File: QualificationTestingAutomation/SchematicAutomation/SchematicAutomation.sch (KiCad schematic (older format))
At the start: 0 parts

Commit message: schematic is finished a few symbols were added, footprints are almost done, some work needs to be done on the connectors#
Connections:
- net labels added: +5V
- wire segments 0 -> 22
- no-connect marks 0 -> 1
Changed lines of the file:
@@
 $Descr B 17000 11000
 encoding utf-8
-Sheet 1 6
+Sheet 1 18
 Title ""
 Date ""
@@
 $EndDescr
 $Sheet
-S 1350 700  3600 2900
+S 1350 650  3600 2900
 U 5B9C8971
 F0 "IO" 50
@@
 $EndSheet
 $Sheet
-S 6100 800  4400 2800
+S 5450 700  4400 2800
 U 5B9C8983
 F0 "MUXing" 50
@@
 $EndSheet
 $Sheet
-S 11650 1000 4300 2550
+S 10400 900  4300 2550
 U 5B9C8995
-F0 "MSP430" 50
-F1 "MSP430.sch" 50
+F0 "ATMEGA2560" 50
+F1 "ATMEGA2560.sch" 50
+F2 "VBUS" I R 14700 1850 50
+F3 "D+" I R 14700 2000 50
+F4 "D-" I R 14700 2150 50
 $EndSheet
 $Sheet
@@
 $EndSheet
 $Sheet
-S 6750 5450 3900 3100
+S 5750 5350 3900 3100
 U 5BCA1CB6
 F0 "MUXing-2" 50
 F1 "MUXing-2.sch" 50
 $EndSheet
+$Sheet
+S 10050 4850 4000 2350
+U 5BB9E3C7
+F0 "RS232" 50
+F1 "RS232.sch" 50
+F2 "DM_1" I R 14050 5900 50
+F3 "DP_1" I R 14050 5800 50
+F4 "DM_2" I R 14050 6250 50
+F5 "DP_2" I R 14050 6350 50
+F6 "DP_3" I R 14050 6550 50
+F7 "DM_3" I R 14050 6650 50
+$EndSheet
+$Sheet
+S 15050 5450 2600 1600
+U 5BE528E5
+F0 "USBInterface" 50
+F1 "USB.sch" 50
+F2 "DM1" I L 15050 5900 50
+F3 "DP1" I L 15050 6000 50
+F4 "DM2" I L 15050 6150 50
+F5 "DP2" I L 15050 6300 50
+F6 "DP3" I L 15050 6550 50
+F7 "DM3" I L 15050 6650 50
+F8 "DP4" I L 15050 5550 50
+F9 "DM4" I L 15050 5650 50
+$EndSheet
+Wire Wire Line
+	14700 2150 14550 2150
+Wire Wire Line
+	14550 2150 14550 5650
+Wire Wire Line
+	14550 5650 15050 5650
+Wire Wire Line
+	15050 5550 14850 5550
+Wire Wire Line
+	14850 5550 14850 2000
+Wire Wire Line
+	14850 2000 14700 2000
+Wire Wire Line
+	15050 5900 14450 5900
+Wire Wire Line
+	14450 5900 14450 5800
+Wire Wire Line
+	14450 5800 14050 5800
+Wire Wire Line
+	15050 6000 14350 6000
+Wire Wire Line
+	14350 6000 14350 5900
+Wire Wire Line
+	14350 5900 14050 5900
+Wire Wire Line
+	15050 6150 14150 6150
+Wire Wire Line
+	14150 6150 14150 6250
+Wire Wire Line
+	14150 6250 14050 6250
+Wire Wire Line
+	15050 6300 14150 6300
+Wire Wire Line
+	14150 6300 14150 6350
+Wire Wire Line
+	14150 6350 14050 6350
+Wire Wire Line
+	15050 6550 14050 6550
+Wire Wire Line
+	15050 6650 14050 6650
+Wire Wire Line
+	14700 1850 14900 1850
+Wire Wire Line
+	14900 1850 14900 1800
+$Comp
+L power:+5V #PWR0291
+U 1 1 5BE75681
+P 14900 1800
+F 0 "#PWR0291" H 14900 1650 50  0001 C CNN
+F 1 "+5V" H 14915 1973 50  0000 C CNN
+F 2 "" H 14900 1800 50  0001 C CNN
+F 3 "" H 14900 1800 50  0001 C CNN
+	1    14900 1800
+	1    0    0    -1
+$EndComp
+NoConn ~ 15750 5650
 $EndSCHEMATC

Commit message: C WPCB was started and the schematic is full, I am thinking of implementing the UART test using analog muxes.
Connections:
- net labels added: D1+, D1-, D2+, D2-, D3+, D3-
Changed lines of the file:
@@
 $Descr B 17000 11000
 encoding utf-8
-Sheet 1 18
+Sheet 1 16
 Title ""
 Date ""
@@
 $EndDescr
 $Sheet
-S 1350 650  3600 2900
+S 950  2050 3600 2900
 U 5B9C8971
 F0 "IO" 50
@@
 $EndSheet
 $Sheet
-S 5450 700  4400 2800
+S 5050 2100 4400 2800
 U 5B9C8983
-F0 "MUXing" 50
-F1 "MUXingsch.sch" 50
+F0 "OBD" 50
+F1 "OBD.sch" 50
 $EndSheet
 $Sheet
-S 10400 900  4300 2550
+S 10000 2300 4300 2550
 U 5B9C8995
 F0 "ATMEGA2560" 50
 F1 "ATMEGA2560.sch" 50
-F2 "VBUS" I R 14700 1850 50
-F3 "D+" I R 14700 2000 50
-F4 "D-" I R 14700 2150 50
+F2 "VBUS" I R 14300 3250 50
+F3 "D+" I R 14300 3400 50
+F4 "D-" I R 14300 3550 50
 $EndSheet
 $Sheet
-S 1950 5600 3300 3050
+S 1550 7000 3300 3050
 U 5BA2CD36
 F0 "Power" 50
@@
 $EndSheet
 $Sheet
-S 5750 5350 3900 3100
+S 5350 6750 3900 3100
 U 5BCA1CB6
 F0 "MUXing-2" 50
@@
 $EndSheet
 $Sheet
-S 10050 4850 4000 2350
+S 9650 6250 4000 2350
 U 5BB9E3C7
 F0 "RS232" 50
 F1 "RS232.sch" 50
-F2 "DM_1" I R 14050 5900 50
-F3 "DP_1" I R 14050 5800 50
-F4 "DM_2" I R 14050 6250 50
-F5 "DP_2" I R 14050 6350 50
-F6 "DP_3" I R 14050 6550 50
-F7 "DM_3" I R 14050 6650 50
+F2 "DM_1" I R 13650 7300 50
+F3 "DP_1" I R 13650 7200 50
+F4 "DM_2" I R 13650 7650 50
+F5 "DP_2" I R 13650 7750 50
+F6 "DP_3" I R 13650 7950 50
+F7 "DM_3" I R 13650 8050 50
 $EndSheet
 $Sheet
-S 15050 5450 2600 1600
+S 14650 6850 2600 1600
 U 5BE528E5
 F0 "USBInterface" 50
 F1 "USB.sch" 50
-F2 "DM1" I L 15050 5900 50
-F3 "DP1" I L 15050 6000 50
-F4 "DM2" I L 15050 6150 50
-F5 "DP2" I L 15050 6300 50
-F6 "DP3" I L 15050 6550 50
-F7 "DM3" I L 15050 6650 50
-F8 "DP4" I L 15050 5550 50
-F9 "DM4" I L 15050 5650 50
+F2 "DM1" I L 14650 7300 50
+F3 "DP1" I L 14650 7400 50
+F4 "DM2" I L 14650 7550 50
+F5 "DP2" I L 14650 7700 50
+F6 "DP3" I L 14650 7950 50
+F7 "DM3" I L 14650 8050 50
+F8 "DP4" I L 14650 6950 50
+F9 "DM4" I L 14650 7050 50
 $EndSheet
 Wire Wire Line
-	14700 2150 14550 2150
+	14300 3550 14150 3550
 Wire Wire Line
-	14550 2150 14550 5650
+	14150 3550 14150 7050
 Wire Wire Line
-	14550 5650 15050 5650
+	14150 7050 14650 7050
 Wire Wire Line
-	15050 5550 14850 5550
+	14650 6950 14450 6950
 Wire Wire Line
-	14850 5550 14850 2000
+	14450 6950 14450 3400
 Wire Wire Line
-	14850 2000 14700 2000
+	14450 3400 14300 3400
 Wire Wire Line
-	15050 5900 14450 5900
+	14650 7300 14050 7300
 Wire Wire Line
-	14450 5900 14450 5800
+	14050 7300 14050 7200
 Wire Wire Line
-	14450 5800 14050 5800
+	14050 7200 13650 7200
 Wire Wire Line
-	15050 6000 14350 6000
+	14650 7400 13950 7400
 Wire Wire Line
-	14350 6000 14350 5900
+	13950 7400 13950 7300
 Wire Wire Line
-	14350 5900 14050 5900
+	13950 7300 13650 7300
 Wire Wire Line
-	15050 6150 14150 6150
+	14650 7550 13750 7550
 Wire Wire Line
-	14150 6150 14150 6250
+	13750 7550 13750 7650
 Wire Wire Line
-	14150 6250 14050 6250
+	13750 7650 13650 7650
 Wire Wire Line
-	15050 6300 14150 6300
+	14650 7700 13750 7700
 Wire Wire Line
-	14150 6300 14150 6350
+	13750 7700 13750 7750
 Wire Wire Line
-	14150 6350 14050 6350
+	13750 7750 13650 7750
 Wire Wire Line
-	15050 6550 14050 6550
+	14650 7950 13650 7950
 Wire Wire Line
-	15050 6650 14050 6650
+	14650 8050 13650 8050
 Wire Wire Line
-	14700 1850 14900 1850
+	14300 3250 14500 3250
 Wire Wire Line
-	14900 1850 14900 1800
+	14500 3250 14500 3200
 $Comp
 L power:+5V #PWR0291
 U 1 1 5BE75681
-P 14900 1800
-F 0 "#PWR0291" H 14900 1650 50  0001 C CNN
-F 1 "+5V" H 14915 1973 50  0000 C CNN
-F 2 "" H 14900 1800 50  0001 C CNN
-F 3 "" H 14900 1800 50  0001 C CNN
-	1    14900 1800
+P 14500 3200
+F 0 "#PWR0291" H 14500 3050 50  0001 C CNN
+F 1 "+5V" H 14515 3373 50  0000 C CNN
+F 2 "" H 14500 3200 50  0001 C CNN
+F 3 "" H 14500 3200 50  0001 C CNN
+	1    14500 3200
 	1    0    0    -1
 $EndComp
-NoConn ~ 15750 5650
+NoConn ~ 15350 7050
+Text Label 14050 7200 0    50   ~ 0
+D1+
+Text Label 13950 7300 0    50   ~ 0
+D1-
+Text Label 14000 7700 0    50   ~ 0
+D2+
+Text Label 14050 7550 0    50   ~ 0
+D2-
+Text Label 14050 8050 0    50   ~ 0
+D3-
+Text Label 14050 7950 0    50   ~ 0
+D3+
 $EndSCHEMATC

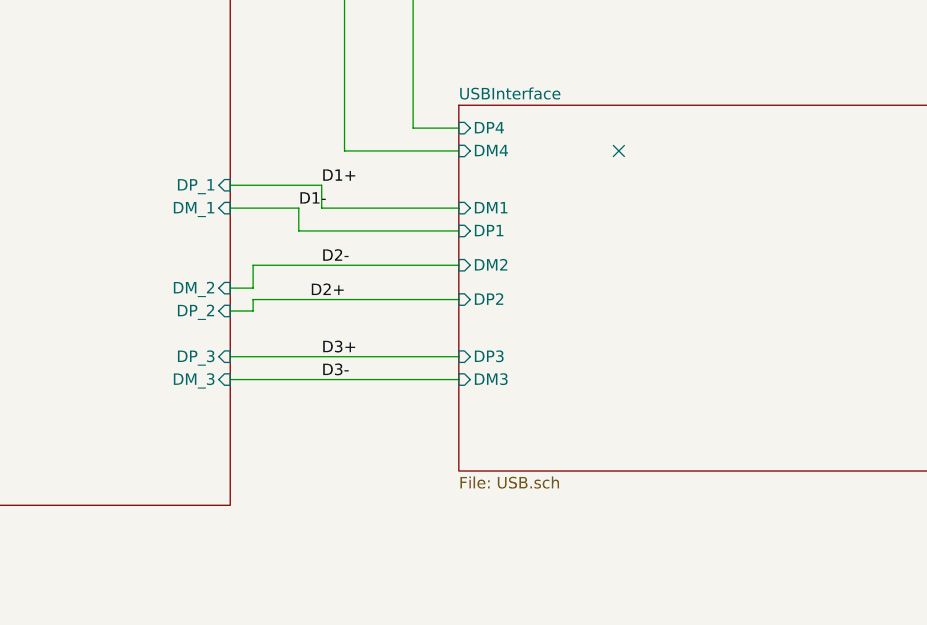
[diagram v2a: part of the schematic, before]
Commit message: Added Schematic Libraries
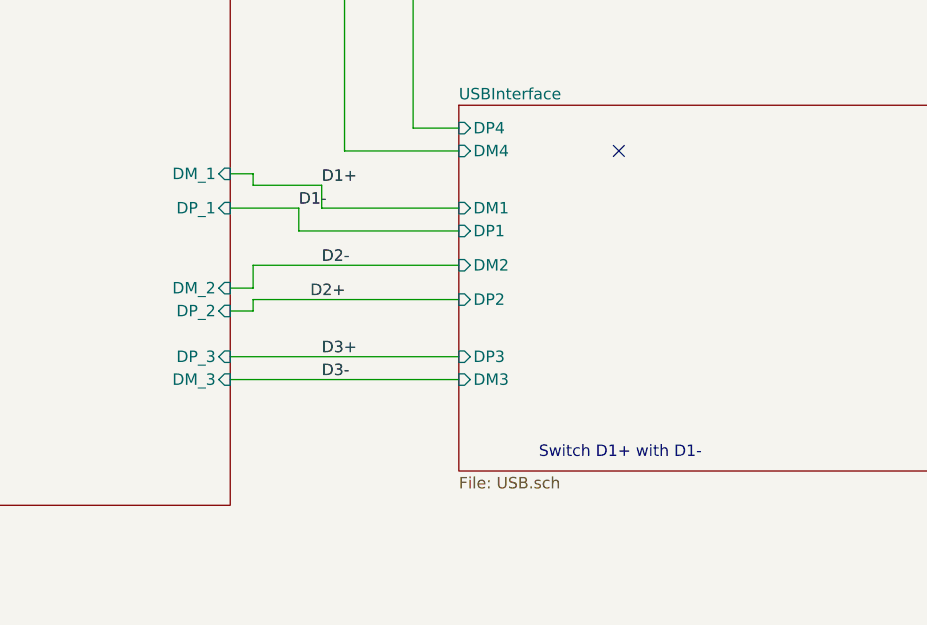
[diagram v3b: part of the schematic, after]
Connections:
- wire segments 22 -> 24
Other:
- note added: "Switch D1+ with D1-\n"
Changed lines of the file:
@@
 F0 "RS232" 50
 F1 "RS232.sch" 50
-F2 "DM_1" I R 13650 7300 50
-F3 "DP_1" I R 13650 7200 50
+F2 "DM_1" I R 13650 7150 50
+F3 "DP_1" I R 13650 7300 50
 F4 "DM_2" I R 13650 7650 50
 F5 "DP_2" I R 13650 7750 50
@@
 Wire Wire Line
 	14050 7300 14050 7200
-Wire Wire Line
-	14050 7200 13650 7200
 Wire Wire Line
 	14650 7400 13950 7400
@@
 Text Label 14050 7950 0    50   ~ 0
 D3+
+Text Notes 15000 8400 0    50   ~ 0
+Switch D1+ with D1-\n
+Wire Wire Line
+	14050 7200 13750 7200
+Wire Wire Line
+	13750 7200 13750 7150
+Wire Wire Line
+	13750 7150 13650 7150
 $EndSCHEMATC

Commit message: CLEANED UP THE SCHEMATICS ADDED NEADED FIXES FOUND ON THE BOARD
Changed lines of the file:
@@
 $EndSheet
 $Sheet
-S 1550 7000 3300 3050
+S 800  6450 3300 3050
 U 5BA2CD36
 F0 "Power" 50
@@
 $EndSheet
 $Sheet
-S 5350 6750 3900 3100
+S 4650 6450 3900 3100
 U 5BCA1CB6
 F0 "MUXing-2" 50
@@
 $EndSheet
 $Sheet
-S 14650 6850 2600 1600
+S 14650 6850 1500 1350
 U 5BE528E5
 F0 "USBInterface" 50
